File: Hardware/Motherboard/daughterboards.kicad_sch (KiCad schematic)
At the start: 21 parts

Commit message: Switch the compiler to Java
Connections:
- net CHANGEOUT renamed OUT_RX_ID
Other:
- note added: "7 WEN2 9 ~{WEN1} 11 ~{WEN0}"
- note removed: "WEN2 ~{WEN1} ~{WEN0}"
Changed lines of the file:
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@@
   (no_connect (at 151.13 170.18))
   (no_connect (at 151.13 167.64))
-  (bus_entry (at 83.82 68.58) (size 2.54 -2.54)
+  (bus_entry (at 86.36 68.58) (size 2.54 -2.54)
     (stroke (width 0) (type default) (color 0 0 0 0))
   )
@@
     (stroke (width 0) (type default) (color 0 0 0 0))
   )
-  (bus_entry (at 83.82 66.04) (size 2.54 -2.54)
+  (bus_entry (at 86.36 66.04) (size 2.54 -2.54)
     (stroke (width 0) (type default) (color 0 0 0 0))
   )
@@
     (stroke (width 0) (type default) (color 0 0 0 0))
   )
-  (bus (pts (xy 86.36 54.61) (xy 86.36 63.5))
+  (bus (pts (xy 88.9 54.61) (xy 88.9 63.5))
     (stroke (width 0) (type default) (color 0 0 0 0))
   )
@@
     (stroke (width 0) (type default) (color 0 0 0 0))
   )
-  (wire (pts (xy 69.85 66.04) (xy 83.82 66.04))
+  (wire (pts (xy 69.85 66.04) (xy 86.36 66.04))
     (stroke (width 0) (type default) (color 0 0 0 0))
   )
@@
     (stroke (width 0) (type default) (color 0 0 0 0))
   )
-  (wire (pts (xy 38.1 118.11) (xy 53.34 118.11))
+  (wire (pts (xy 40.64 118.11) (xy 53.34 118.11))
     (stroke (width 0) (type default) (color 0 0 0 0))
   )
@@
     (stroke (width 0) (type default) (color 0 0 0 0))
   )
-  (wire (pts (xy 69.85 68.58) (xy 83.82 68.58))
+  (wire (pts (xy 69.85 68.58) (xy 86.36 68.58))
     (stroke (width 0) (type default) (color 0 0 0 0))
   )
@@
     (stroke (width 0) (type default) (color 0 0 0 0))
   )
+  (wire (pts (xy 69.85 63.5) (xy 78.74 63.5))
+    (stroke (width 0) (type default) (color 0 0 0 0))
+  )
   (bus (pts (xy 218.44 17.78) (xy 218.44 20.32))
     (stroke (width 0) (type default) (color 0 0 0 0))
@@
     (stroke (width 0) (type default) (color 0 0 0 0))
   )
+  (wire (pts (xy 40.64 120.65) (xy 53.34 120.65))
+    (stroke (width 0) (type default) (color 0 0 0 0))
+  )
   (bus (pts (xy 40.64 139.7) (xy 40.64 137.16))
     (stroke (width 0) (type default) (color 0 0 0 0))
@@
     (stroke (width 0) (type default) (color 0 0 0 0))
   )
-  (wire (pts (xy 38.1 115.57) (xy 53.34 115.57))
+  (wire (pts (xy 40.64 115.57) (xy 53.34 115.57))
     (stroke (width 0) (type default) (color 0 0 0 0))
   )
@@
     (stroke (width 0) (type default) (color 0 0 0 0))
   )
-  (bus (pts (xy 40.64 54.61) (xy 86.36 54.61))
+  (bus (pts (xy 40.64 54.61) (xy 88.9 54.61))
     (stroke (width 0) (type default) (color 0 0 0 0))
   )
@@
     (stroke (width 0) (type default) (color 0 0 0 0))
   )
-  (bus (pts (xy 86.36 63.5) (xy 86.36 66.04))
+  (bus (pts (xy 88.9 63.5) (xy 88.9 66.04))
     (stroke (width 0) (type default) (color 0 0 0 0))
   )
@@
     (stroke (width 0) (type default) (color 0 0 0 0))
   )
-  (text "WEN2\n~{WEN1}\n~{WEN0}" (at 229.87 109.22 180)
-    (effects (font (size 1.5 1.5)) (justify right bottom))
-  )
   (text "For Debugging from the ACC" (at 144.78 259.08 0)
     (effects (font (size 1.27 1.27)) (justify left bottom))
   )
+  (text "7  WEN2\n9  ~{WEN1}\n11 ~{WEN0}" (at 228.6 109.22 180)
+    (effects (font (size 1.5 1.5)) (justify right bottom))
+  )
   (text "~{REN}" (at 181.61 100.33 0)
     (effects (font (size 1.27 1.27)) (justify left bottom))
@@
     (effects (font (size 2.54 2.54)) (justify left bottom))
   )
-  (text "WEN2\n~{WEN1}\n~{WEN0}" (at 124.46 110.49 180)
+  (text "7  WEN2\n9  ~{WEN1}\n11 ~{WEN0}" (at 127 110.49 180)
     (effects (font (size 1.5 1.5)) (justify right bottom))
   )
@@
     (effects (font (size 1.27 1.27)) (justify left bottom))
   )
+  (label "OUT_RX_ID" (at 41.91 120.65 0)
+    (effects (font (size 1.27 1.27)) (justify left bottom))
+  )
   (label "~{CARRY_WE}" (at 53.34 115.57 180)
     (effects (font (size 1.27 1.27)) (justify right bottom))
@@
     (effects (font (size 1.27 1.27)) (justify left bottom))
   )
-  (label "CHANGEOUT" (at 53.34 120.65 180)
-    (effects (font (size 1.27 1.27)) (justify right bottom))
-  )
   (label "MEM_ADDR5" (at 203.2 27.94 0)
     (effects (font (size 1.27 1.27)) (justify left bottom))
@@
     (effects (font (size 1.27 1.27)) (justify right))
   )
+  (hierarchical_label "OUT_RX_ID" (shape input) (at 40.64 120.65 180)
+    (effects (font (size 1.27 1.27)) (justify right))
+  )
   (hierarchical_label "CLK" (shape input) (at 212.09 55.88 0)
     (effects (font (size 1.27 1.27)) (justify left))
@@
     (effects (font (size 1.27 1.27)) (justify right))
   )
-  (hierarchical_label "~{L}" (shape input) (at 38.1 115.57 180)
+  (hierarchical_label "~{L}" (shape input) (at 40.64 115.57 180)
     (effects (font (size 1.27 1.27)) (justify right))
   )
@@
     (effects (font (size 1.27 1.27)) (justify right))
   )
-  (hierarchical_label "CARRY" (shape input) (at 38.1 118.11 180)
+  (hierarchical_label "CARRY" (shape input) (at 40.64 118.11 180)
     (effects (font (size 1.27 1.27)) (justify right))
   )
@@
     (effects (font (size 1.27 1.27)) (justify left))
   )
+  (hierarchical_label "~{MEM_WE}" (shape input) (at 78.74 63.5 0)
+    (effects (font (size 1.27 1.27)) (justify left))
+  )

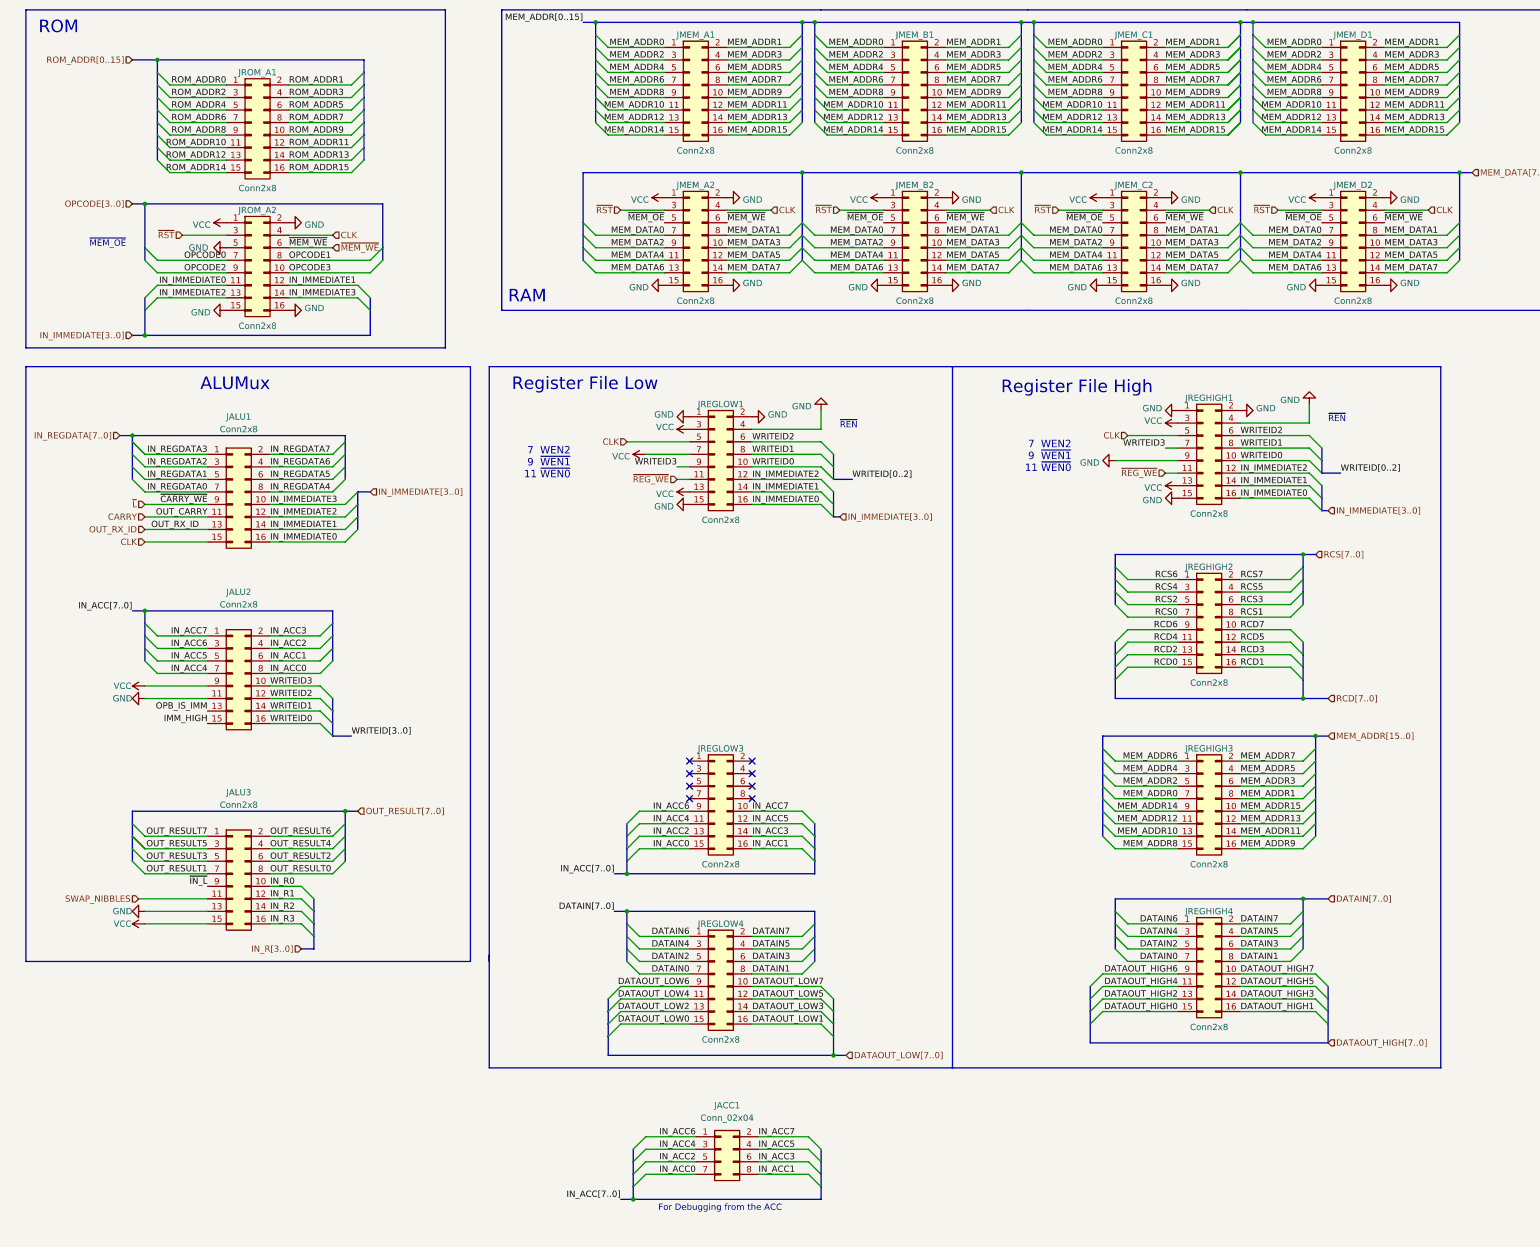
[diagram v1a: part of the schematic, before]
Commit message: Motherboard Schematic Major Updates:  - Skip implemented  - Memory WB implemented Also, the JavaAssembler was somewhat updated but isn't done yet.
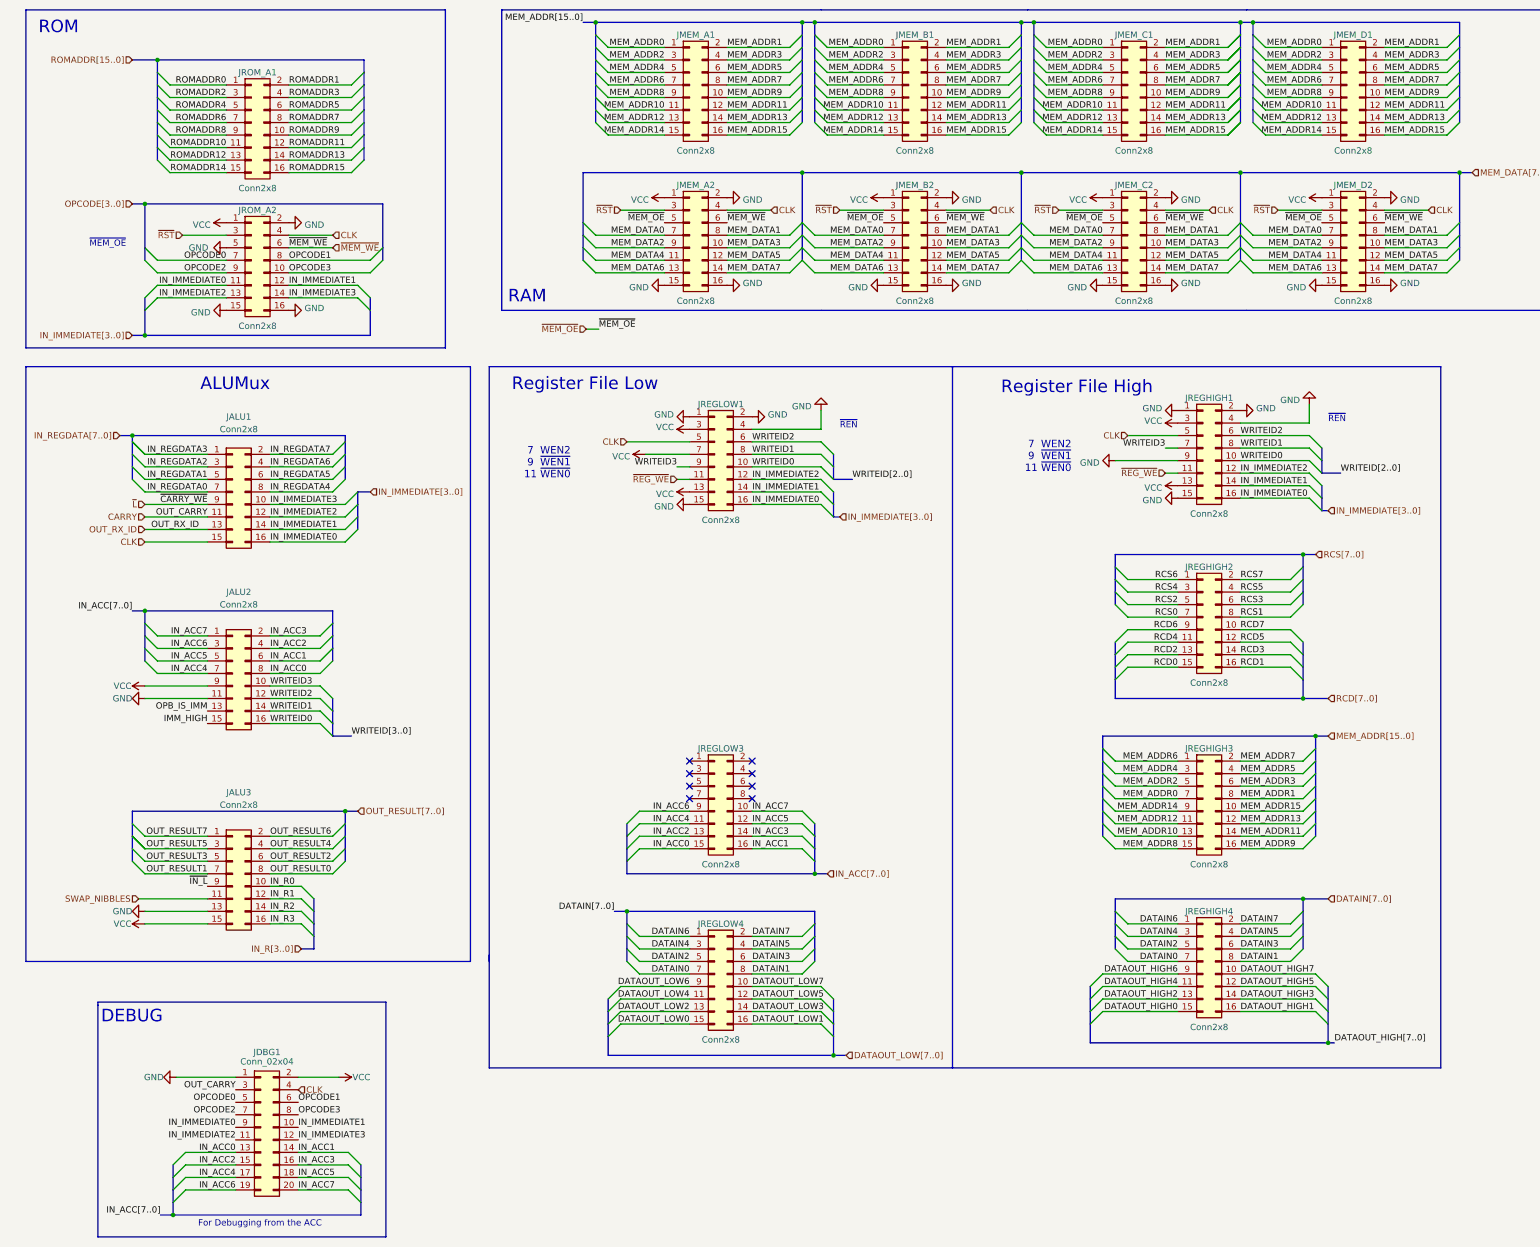
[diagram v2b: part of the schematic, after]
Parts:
- JDBG1: renamed from JACC1; footprint Connector_PinHeader_2.54mm:PinHeader_2x04_P2.54mm_Vertical -> Connector_PinSocket_2.54mm:PinSocket_2x10_P2.54mm_Vertical; symbol Connector_Generic:Conn_02x04_Odd_Even -> Connector_Generic:Conn_02x10_Odd_Even
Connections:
- net CARRY: now also JDBG1.3 (Pin_3)
- net CLK: now also JDBG1.4 (Pin_4)
- net GND: now also JDBG1.1 (Pin_1)
- net IN_ACC0: now also JDBG1.13 (Pin_13); no longer JDBG1.7 (Pin_7)
- net IN_ACC1: now also JDBG1.14 (Pin_14); no longer JDBG1.8 (Pin_8)
- net IN_ACC2: now also JDBG1.15 (Pin_15); no longer JDBG1.5 (Pin_5)
- net IN_ACC3: now also JDBG1.16 (Pin_16); no longer JDBG1.6 (Pin_6)
- net IN_ACC4: now also JDBG1.17 (Pin_17); no longer JDBG1.3 (Pin_3)
- net IN_ACC5: now also JDBG1.18 (Pin_18); no longer JDBG1.4 (Pin_4)
- net IN_ACC6: now also JDBG1.19 (Pin_19); no longer JDBG1.1 (Pin_1)
- net IN_ACC7: now also JDBG1.20 (Pin_20); no longer JDBG1.2 (Pin_2)
- net IN_IMMEDIATE0: now also JDBG1.9 (Pin_9)
- net IN_IMMEDIATE1: now also JDBG1.10 (Pin_10)
- net IN_IMMEDIATE2: now also JDBG1.11 (Pin_11)
- net IN_IMMEDIATE3: now also JDBG1.12 (Pin_12)
- net OPCODE0: now also JDBG1.5 (Pin_5)
- net OPCODE1: now also JDBG1.6 (Pin_6)
- net OPCODE2: now also JDBG1.7 (Pin_7)
- net OPCODE3: now also JDBG1.8 (Pin_8)
- net VCC: now also JDBG1.2 (Pin_2)
- net ROM_ADDR0 renamed ROMADDR0
- net ROM_ADDR1 renamed ROMADDR1
- net ROM_ADDR10 renamed ROMADDR10
- net ROM_ADDR11 renamed ROMADDR11
- net ROM_ADDR12 renamed ROMADDR12
- net ROM_ADDR13 renamed ROMADDR13
- net ROM_ADDR14 renamed ROMADDR14
- net ROM_ADDR15 renamed ROMADDR15
- net ROM_ADDR2 renamed ROMADDR2
- net ROM_ADDR3 renamed ROMADDR3
- net ROM_ADDR4 renamed ROMADDR4
- net ROM_ADDR5 renamed ROMADDR5
- net ROM_ADDR6 renamed ROMADDR6
- net ROM_ADDR7 renamed ROMADDR7
- net ROM_ADDR8 renamed ROMADDR8
- net ROM_ADDR9 renamed ROMADDR9
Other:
- note added: "DEBUG"
